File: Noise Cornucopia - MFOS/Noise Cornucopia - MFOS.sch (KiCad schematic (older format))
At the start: 85 parts, among them J1 GRNS_3, J10 Q4, J11 Conn_01x01_Female, J12 Q5, J13 Q6, J14 GATE_JMP, J15 White, J16 LP_White, J17 GATE_OUT, J18 HP_White, J19 LED, J2 GRNS_W1, J20 +12V_Conn, J21 GND_Conn?, J22 -12V_Conn, J3 Gate_F_W1, J4 Gate_F_3, J5 Grain, J6 Grain_HP, J7 Q0, J8 Q1, J9 Q2, Q1 2N3904, Q2 2N3904, U1 TL072, U2 TL072, U3 TL072, U4 4024, U5 TL072

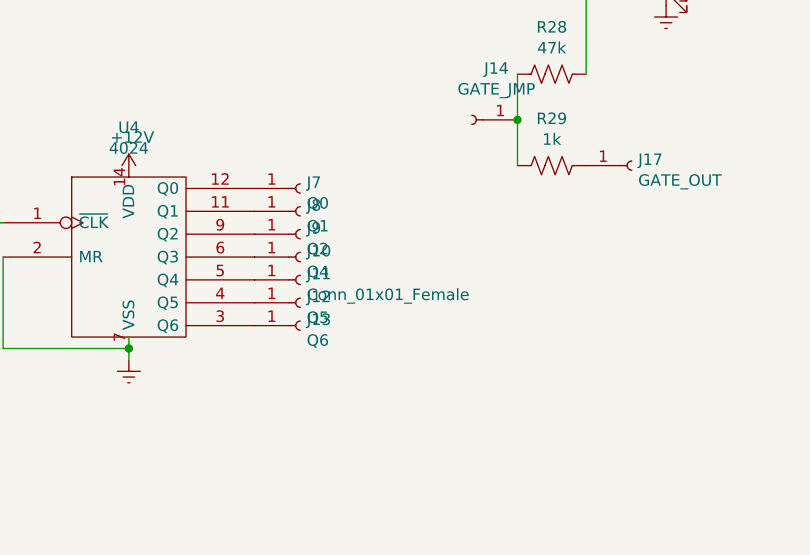
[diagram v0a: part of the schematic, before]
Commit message: added noise pcb
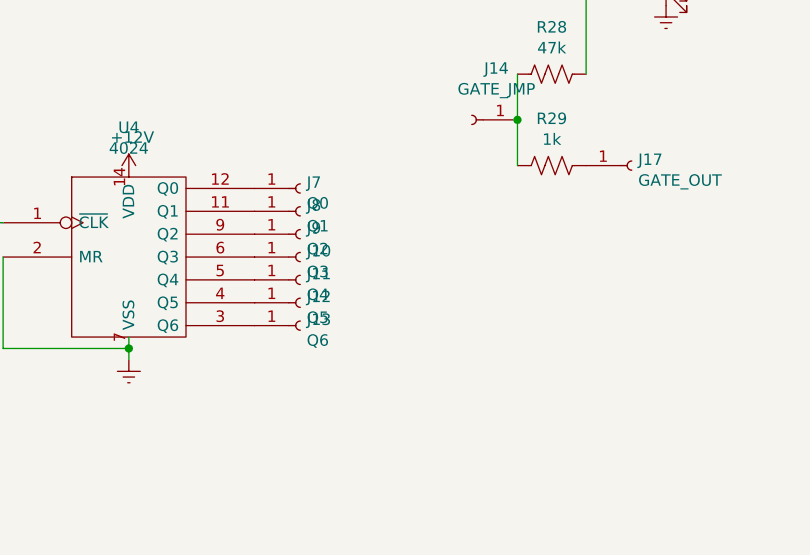
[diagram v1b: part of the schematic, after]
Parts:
- J10: value Q4 -> Q3
- J11: value Conn_01x01_Female -> Q4
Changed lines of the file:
@@
 EESchema Schematic File Version 4
+LIBS:Noise Cornucopia - MFOS-cache
 EELAYER 29 0
 EELAYER END
@@
 P 5500 6500
 F 0 "J10" H 5528 6526 50  0000 L CNN
-F 1 "Q4" H 5528 6435 50  0000 L CNN
+F 1 "Q3" H 5528 6435 50  0000 L CNN
 F 2 "Connector_Wire:SolderWirePad_1x01_Drill1mm" H 5500 6500 50  0001 C CNN
 F 3 "~" H 5500 6500 50  0001 C CNN
@@
 P 5500 6600
 F 0 "J11" H 5528 6626 50  0000 L CNN
-F 1 "Conn_01x01_Female" H 5528 6535 50  0000 L CNN
+F 1 "Q4" H 5528 6535 50  0000 L CNN
 F 2 "Connector_Wire:SolderWirePad_1x01_Drill1mm" H 5500 6600 50  0001 C CNN
 F 3 "~" H 5500 6600 50  0001 C CNN
